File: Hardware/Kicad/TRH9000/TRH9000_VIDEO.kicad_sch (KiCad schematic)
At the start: 34 parts, among them J2 S-Video, J3 Composite, J4 DB15_Female_HighDensity, Q1 BC817, U6 CXA2075M

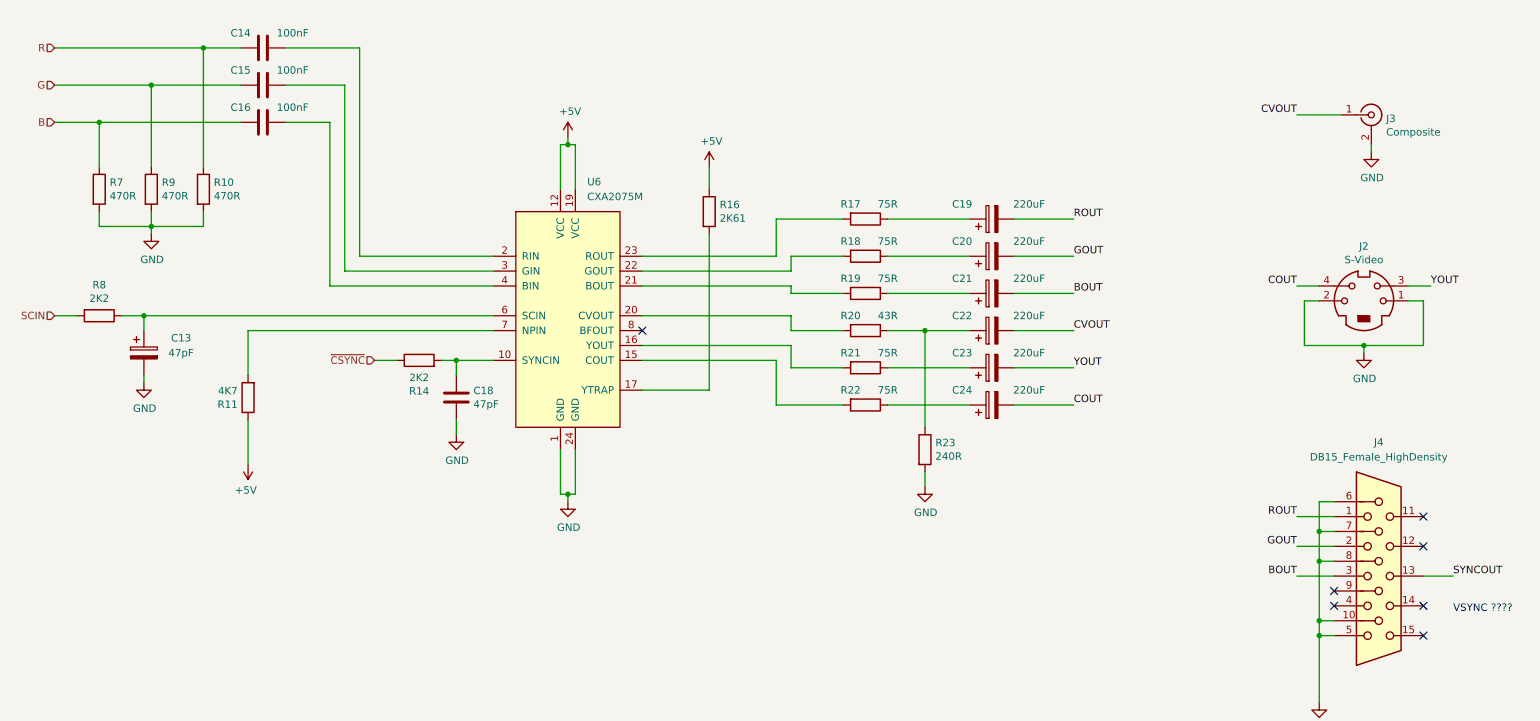
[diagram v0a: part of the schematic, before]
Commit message: Footprint for the V9990
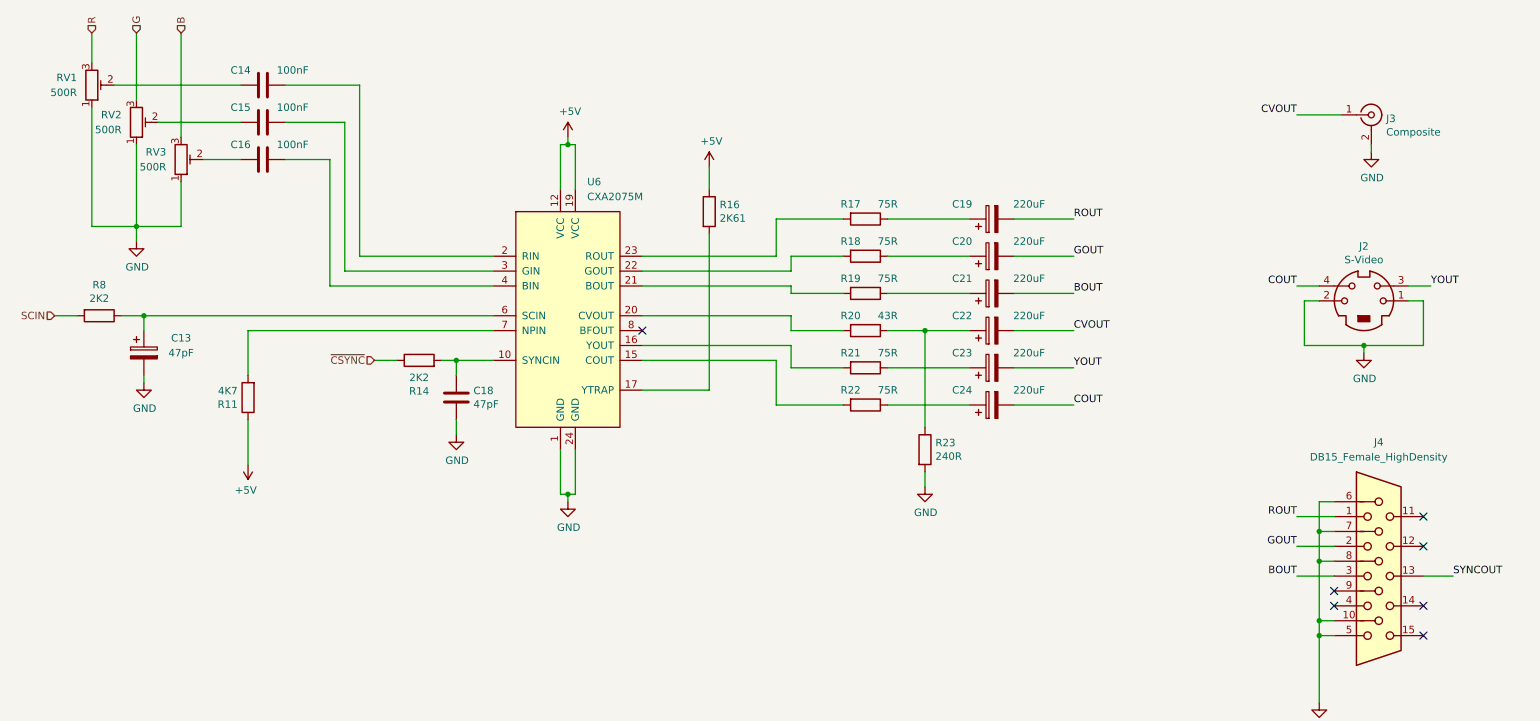
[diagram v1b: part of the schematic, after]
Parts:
- removed R10, R7, R9: 470R, LED_SMD:LED_0805_2012Metric, symbol Device:R
- added RV1, RV2, RV3: 500R, Potentiometer_SMD:Potentiometer_Bourns_3314G_Vertical, symbol Device:R_Potentiometer_Trim
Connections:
- net B: now also RV3.3; no longer C16.2
- net G: now also RV2.3; no longer C15.2
- net GND: now also RV1.1, RV2.1, RV3.1
- net R: now also RV1.3; no longer C14.2
- new net: C15.2, RV2.2
- new net: C14.2, RV1.2
- new net: C16.2, RV3.2
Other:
- note removed: "VSYNC ????"
- moved on the sheet: C14, C15, C16

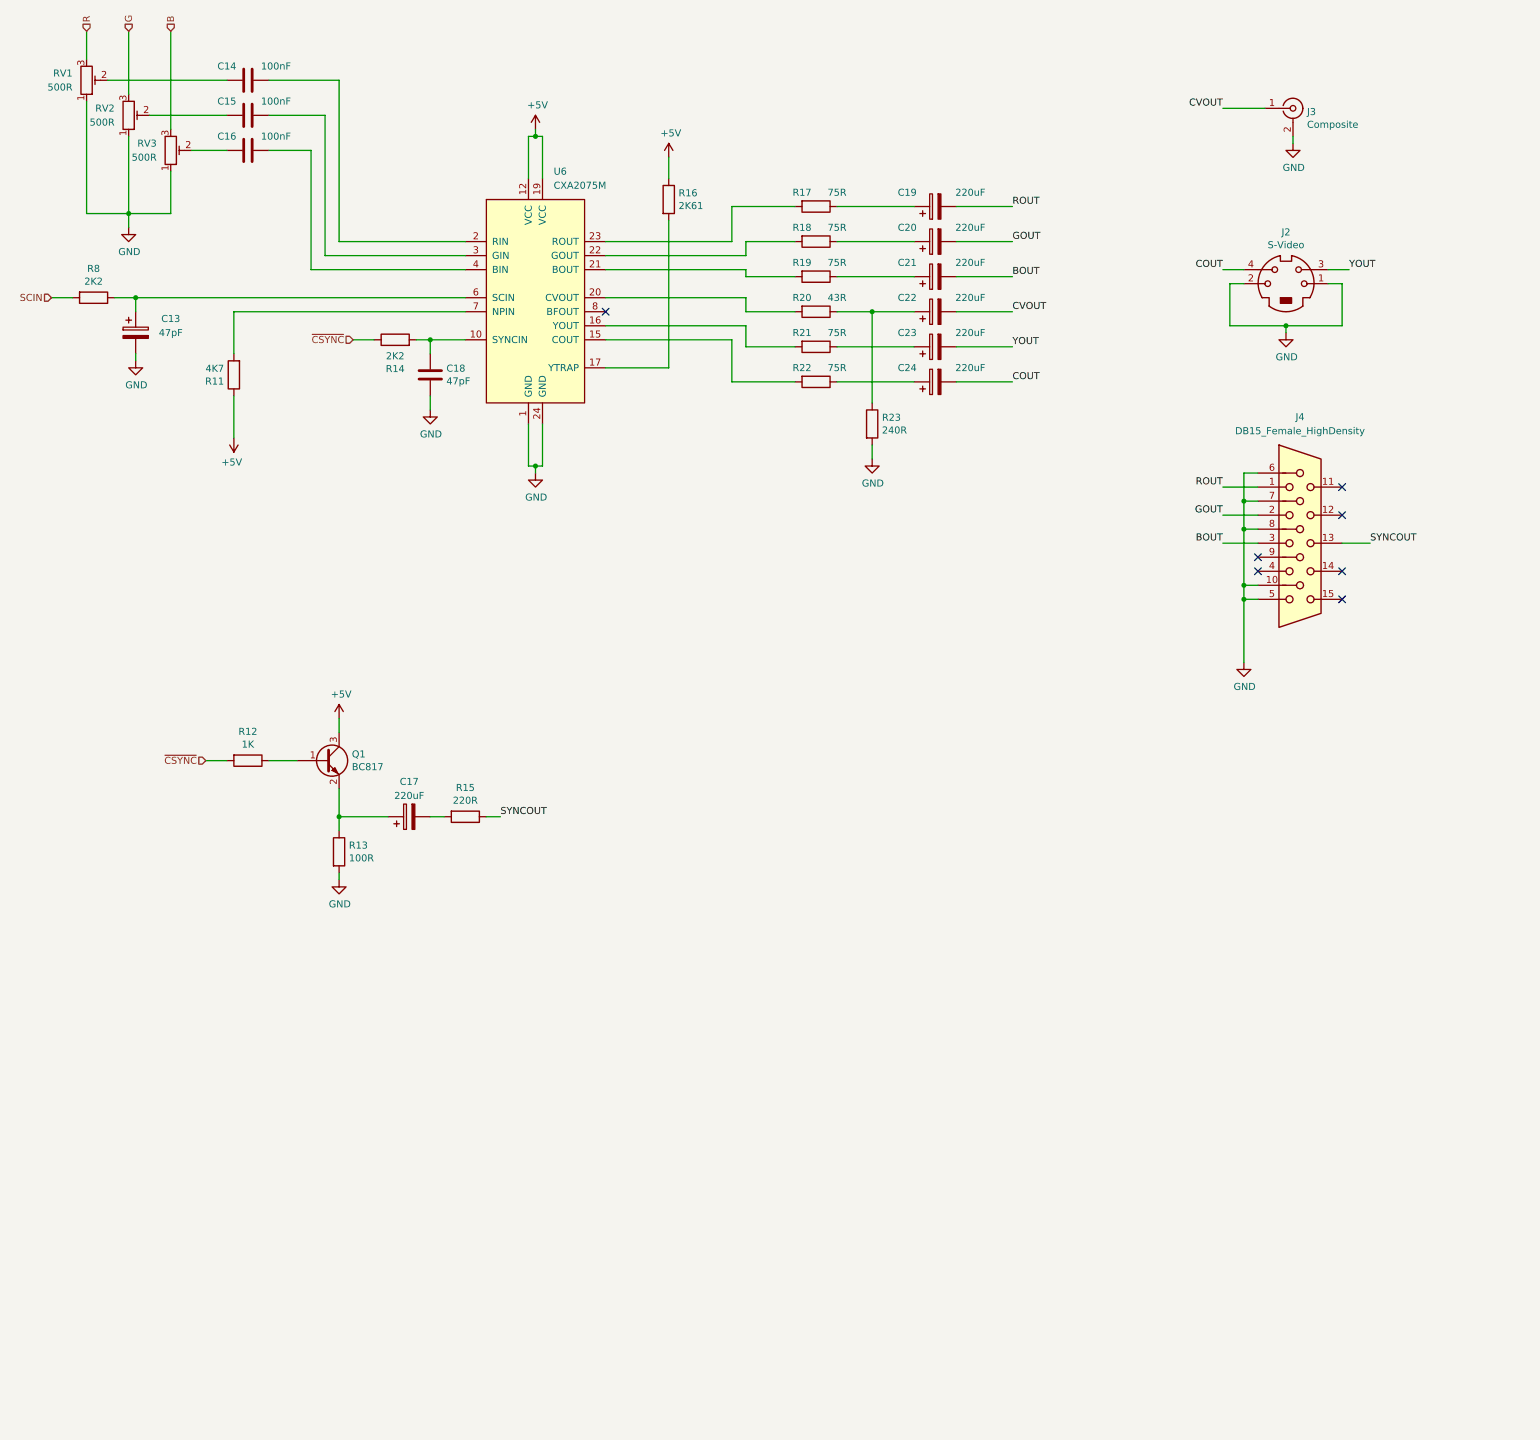
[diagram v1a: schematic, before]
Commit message: Trimpots for the RGB coming from V9990
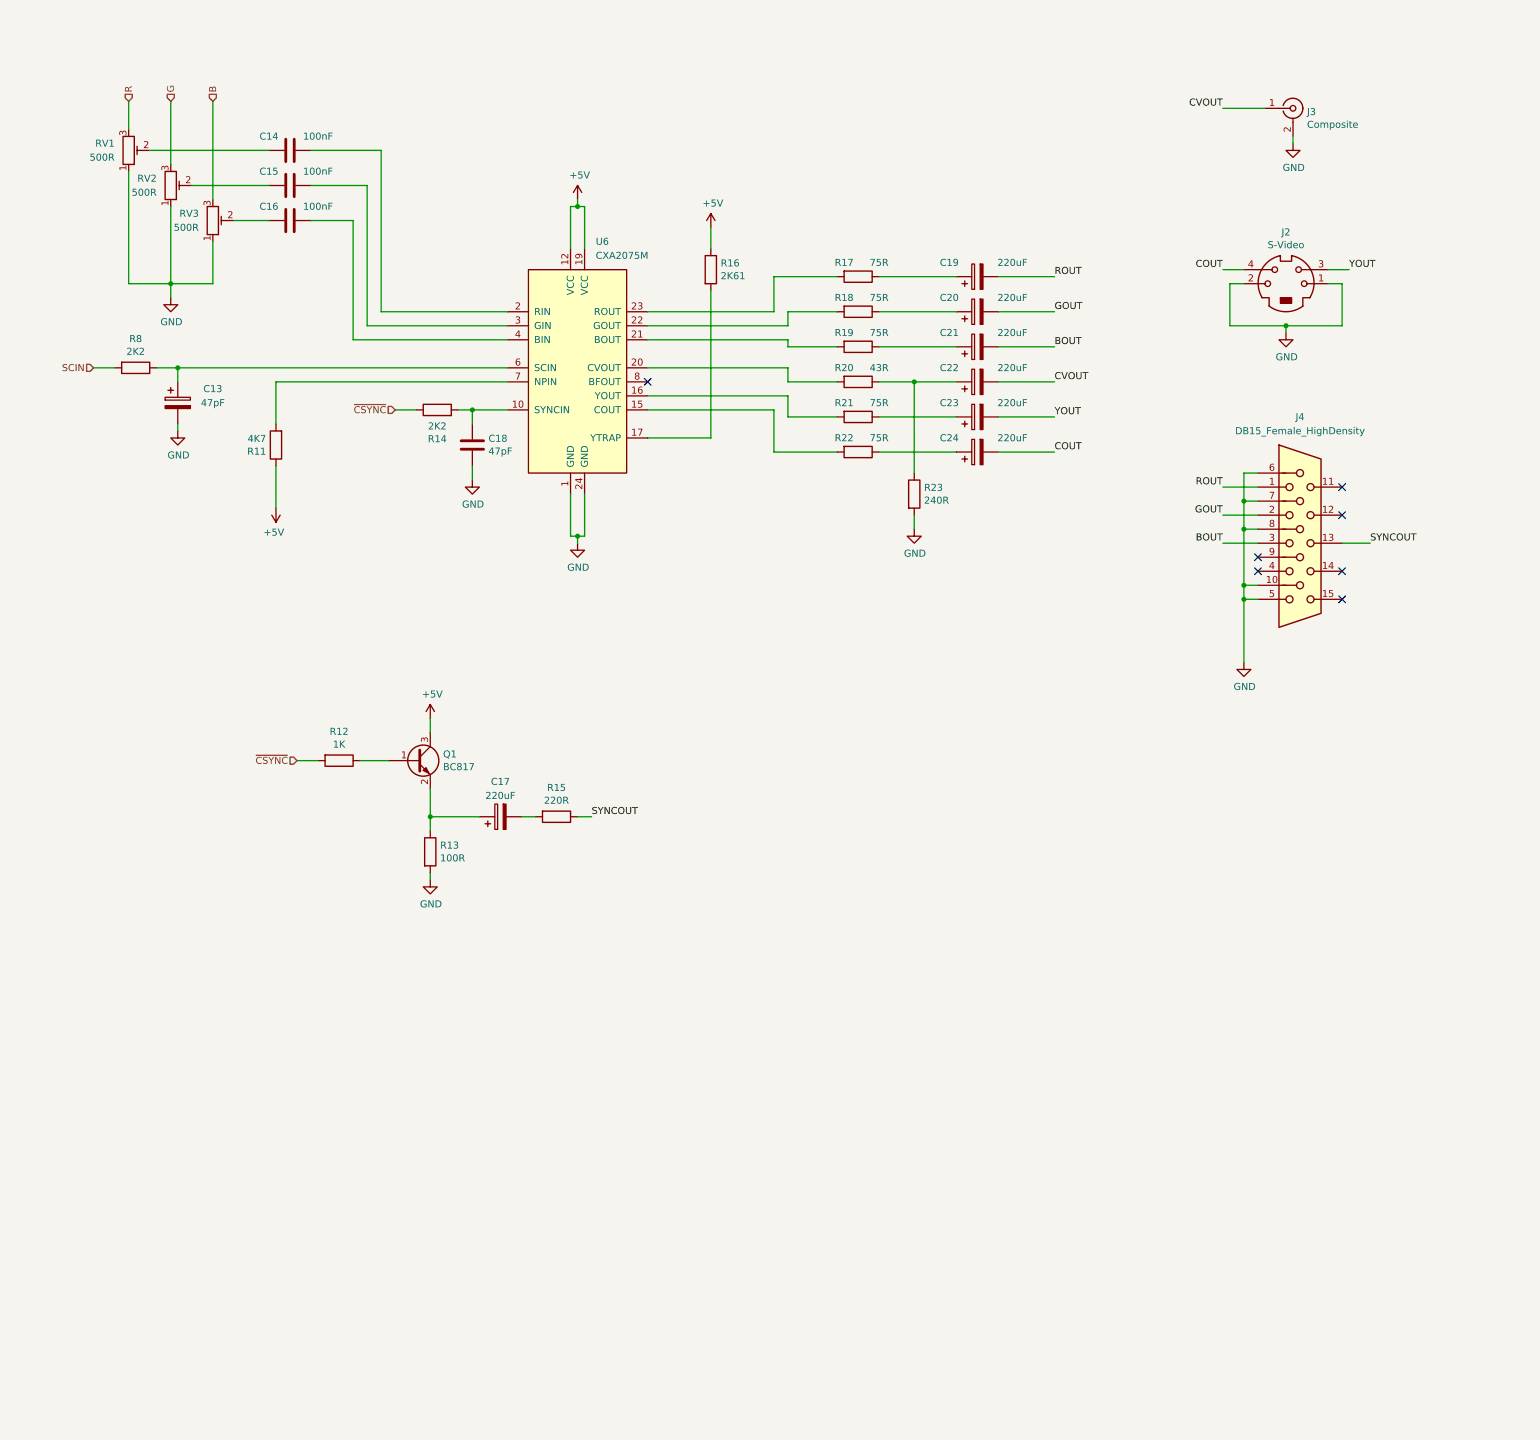
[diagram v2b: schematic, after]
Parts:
- J4: footprint (none) -> Connector_Dsub:DSUB-15-HD_Female_Horizontal_P2.29x1.98mm_EdgePinOffset3.03mm_Housed_MountingHolesOffset4.94mm
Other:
- moved on the sheet: C13, C14, C15, C16, C17, C18, C19, C20, C21, C22, C23, C24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

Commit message: REV0 - Footprint Review
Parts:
- J2: footprint Ddraig:MINI-DIN-4-TE_5749181-1 -> trh9000:MINI-DIN-4-TE_5749181-1
- J3: footprint Ddraig:KLPX0848A2RG -> trh9000:KLPX0848A2RG
- R11, R12, R13, R14, R15, R16, R17, R18, R19, R20, R21, R22, R23: footprint LED_SMD:LED_0805_2012Metric -> Resistor_SMD:R_0805_2012Metric
- R8: footprint LED_SMD:LED_0805_2012Metric -> Resistor_SMD:R_0815_2038Metric
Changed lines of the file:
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@@
     (property "Reference" "R21" (id 0) (at 166.37 85.09 90))
     (property "Value" "75R" (id 1) (at 172.72 85.09 90))
-    (property "Footprint" "LED_SMD:LED_0805_2012Metric" (id 2) (at 168.91 85.852 90)
+    (property "Footprint" "Resistor_SMD:R_0805_2012Metric" (id 2) (at 168.91 85.852 90)
       (effects (font (size 1.27 1.27)) hide)
     )
@@
       (effects (font (size 1.27 1.27)) (justify left))
     )
-    (property "Footprint" "LED_SMD:LED_0805_2012Metric" (id 2) (at 89.662 166.37 90)
+    (property "Footprint" "Resistor_SMD:R_0805_2012Metric" (id 2) (at 89.662 166.37 90)
       (effects (font (size 1.27 1.27)) hide)
     )
@@
     (property "Reference" "R17" (id 0) (at 166.37 59.69 90))
     (property "Value" "75R" (id 1) (at 172.72 59.69 90))
-    (property "Footprint" "LED_SMD:LED_0805_2012Metric" (id 2) (at 168.91 60.452 90)
+    (property "Footprint" "Resistor_SMD:R_0805_2012Metric" (id 2) (at 168.91 60.452 90)
       (effects (font (size 1.27 1.27)) hide)
     )
@@
     (property "Reference" "R22" (id 0) (at 166.37 91.44 90))
     (property "Value" "75R" (id 1) (at 172.72 91.44 90))
-    (property "Footprint" "LED_SMD:LED_0805_2012Metric" (id 2) (at 168.91 92.202 90)
+    (property "Footprint" "Resistor_SMD:R_0805_2012Metric" (id 2) (at 168.91 92.202 90)
       (effects (font (size 1.27 1.27)) hide)
     )
@@
     (property "Reference" "R12" (id 0) (at 74.93 144.6022 90))
     (property "Value" "1K" (id 1) (at 74.93 146.9136 90))
-    (property "Footprint" "LED_SMD:LED_0805_2012Metric" (id 2) (at 74.93 148.082 90)
+    (property "Footprint" "Resistor_SMD:R_0805_2012Metric" (id 2) (at 74.93 148.082 90)
       (effects (font (size 1.27 1.27)) hide)
     )
@@
     (property "Reference" "R20" (id 0) (at 166.37 78.74 90))
     (property "Value" "43R" (id 1) (at 172.72 78.74 90))
-    (property "Footprint" "LED_SMD:LED_0805_2012Metric" (id 2) (at 168.91 79.502 90)
+    (property "Footprint" "Resistor_SMD:R_0805_2012Metric" (id 2) (at 168.91 79.502 90)
       (effects (font (size 1.27 1.27)) hide)
     )
@@
       (effects (font (size 1.27 1.27)) (justify left))
     )
-    (property "Footprint" "Ddraig:KLPX0848A2RG" (id 2) (at 247.65 31.75 0)
+    (property "Footprint" "trh9000:KLPX0848A2RG" (id 2) (at 247.65 31.75 0)
       (effects (font (size 1.27 1.27)) hide)
     )
@@
     (property "Reference" "J2" (id 0) (at 246.38 54.1782 0))
     (property "Value" "S-Video" (id 1) (at 246.38 56.4896 0))
-    (property "Footprint" "Ddraig:MINI-DIN-4-TE_5749181-1" (id 2) (at 246.38 63.5 0)
+    (property "Footprint" "trh9000:MINI-DIN-4-TE_5749181-1" (id 2) (at 246.38 63.5 0)
       (effects (font (size 1.27 1.27)) hide)
     )
@@
     (property "Reference" "R14" (id 0) (at 92.71 91.6178 90))
     (property "Value" "2K2" (id 1) (at 92.71 89.3064 90))
-    (property "Footprint" "LED_SMD:LED_0805_2012Metric" (id 2) (at 92.71 88.138 90)
+    (property "Footprint" "Resistor_SMD:R_0805_2012Metric" (id 2) (at 92.71 88.138 90)
       (effects (font (size 1.27 1.27)) hide)
     )
@@
       (effects (font (size 1.27 1.27)) (justify left))
     )
-    (property "Footprint" "LED_SMD:LED_0805_2012Metric" (id 2) (at 177.292 101.6 90)
+    (property "Footprint" "Resistor_SMD:R_0805_2012Metric" (id 2) (at 177.292 101.6 90)
       (effects (font (size 1.27 1.27)) hide)
     )
@@
       (effects (font (size 1.27 1.27)) (justify left))
     )
-    (property "Footprint" "LED_SMD:LED_0805_2012Metric" (id 2) (at 140.462 60.96 90)
+    (property "Footprint" "Resistor_SMD:R_0805_2012Metric" (id 2) (at 140.462 60.96 90)
       (effects (font (size 1.27 1.27)) hide)
     )
@@
     (property "Reference" "R19" (id 0) (at 166.37 72.39 90))
     (property "Value" "75R" (id 1) (at 172.72 72.39 90))
-    (property "Footprint" "LED_SMD:LED_0805_2012Metric" (id 2) (at 168.91 73.152 90)
+    (property "Footprint" "Resistor_SMD:R_0805_2012Metric" (id 2) (at 168.91 73.152 90)
       (effects (font (size 1.27 1.27)) hide)
     )
@@
     (property "Reference" "R15" (id 0) (at 114.3 154.7622 90))
     (property "Value" "220R" (id 1) (at 114.3 157.0736 90))
-    (property "Footprint" "LED_SMD:LED_0805_2012Metric" (id 2) (at 114.3 158.242 90)
+    (property "Footprint" "Resistor_SMD:R_0805_2012Metric" (id 2) (at 114.3 158.242 90)
       (effects (font (size 1.27 1.27)) hide)
     )
@@
     (property "Reference" "R8" (id 0) (at 38.1 73.4822 90))
     (property "Value" "2K2" (id 1) (at 38.1 75.7936 90))
-    (property "Footprint" "LED_SMD:LED_0805_2012Metric" (id 2) (at 38.1 76.962 90)
+    (property "Footprint" "Resistor_SMD:R_0815_2038Metric" (id 2) (at 38.1 76.962 90)
       (effects (font (size 1.27 1.27)) hide)
     )
@@
     (property "Reference" "R18" (id 0) (at 166.37 66.04 90))
     (property "Value" "75R" (id 1) (at 172.72 66.04 90))
-    (property "Footprint" "LED_SMD:LED_0805_2012Metric" (id 2) (at 168.91 66.802 90)
+    (property "Footprint" "Resistor_SMD:R_0805_2012Metric" (id 2) (at 168.91 66.802 90)
       (effects (font (size 1.27 1.27)) hide)
     )
@@
       (effects (font (size 1.27 1.27)) (justify left))
     )
-    (property "Footprint" "LED_SMD:LED_0805_2012Metric" (id 2) (at 65.278 92.71 90)
-      (effects (font (size 1.27 1.27)) hide)
-    )
+    (property "Footprint" "Resistor_SMD:R_0805_2012Metric" (id 2) (at 65.278 92.71 90)
+      (effects (font (size 1.27 1.27)) hide)
+    )
